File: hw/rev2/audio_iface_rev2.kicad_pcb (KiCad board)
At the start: 4 copper layers, 66 x 24.8 mm, 151 parts, among them J1 COAX, J2 CONN_01X02, J3 USBMICROCONN, J4 CONN_01X02, J5 CONN_01X02, J6 COAX, J7 COAX, J9 CONN_01X02, P3 CONN_01X06, U1 LT6241, U2 LTC6242, U3 AK4621, U4 K20X7_QFP64, U5 TPS61252, U6 LP2992AILD-5.0, U7 LTC6242, U8 TPA6130A2, U9 MT29FXX01A, X1 XTAL, X2 ASFLM2-12.288MHZ

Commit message: More routing
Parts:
- added TP12: TP, lib:TP_HOLE, F.Cu at (198.5, 73.0)
- added TP13: TP, lib:TP_HOLE, F.Cu at (199.5, 76.7)
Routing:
- net AGND_IN: track 199.1 -> 195.0 mm, vias 63 -> 62
- net +5VA: track 124.4 -> 125.5 mm, vias 13 -> 15
- net VCOM_VRT: track 36.9 -> 37.8 mm
- net (no net): track 3.38 -> 3.49 mm, vias 4 -> 5
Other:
- board text added: "AGND"
- board text added: "VCOM"

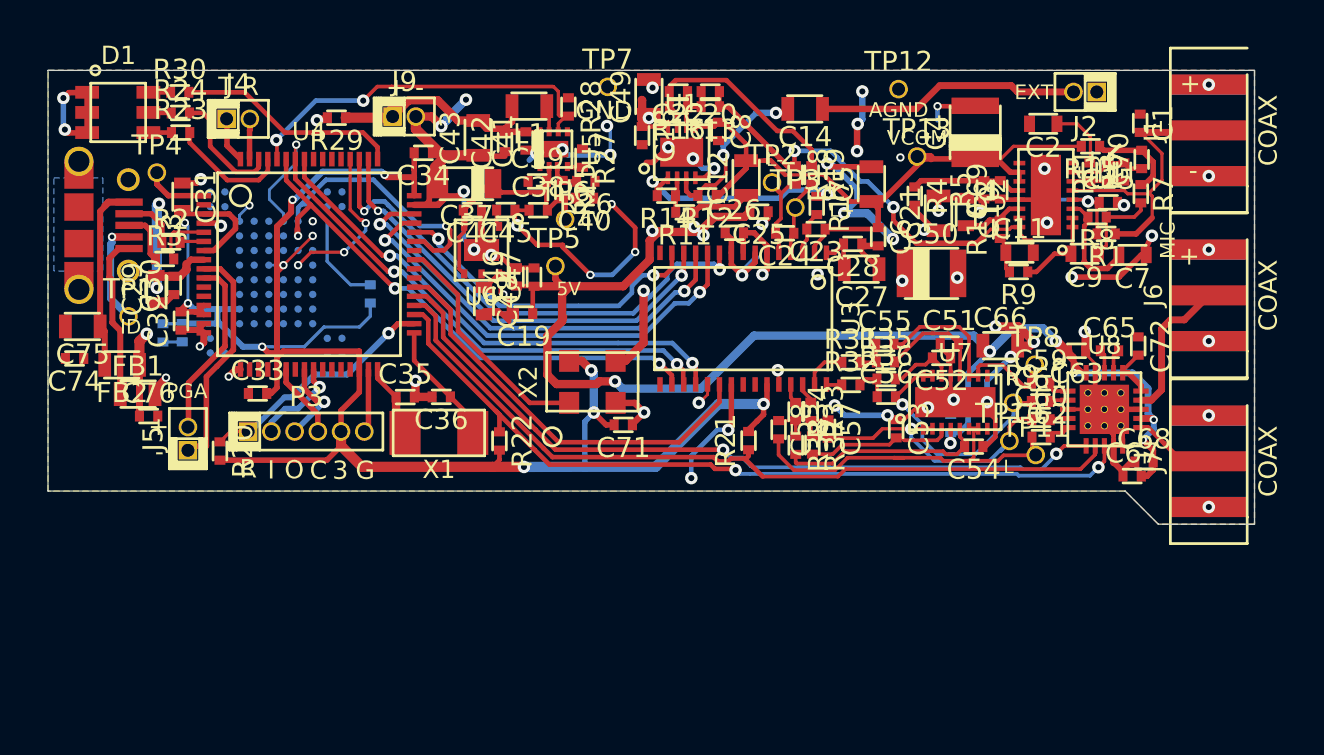
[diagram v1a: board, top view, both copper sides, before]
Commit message: Submitted PCB revision
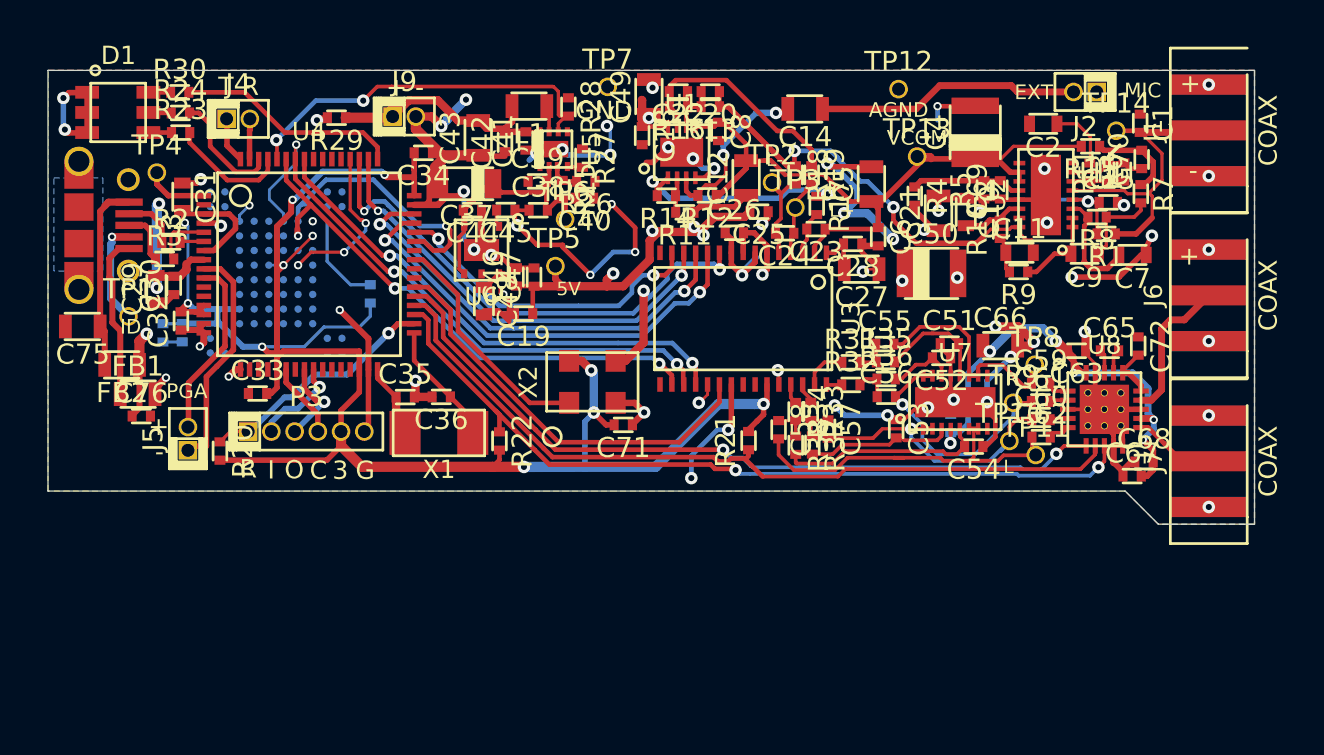
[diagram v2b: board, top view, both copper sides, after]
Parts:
- removed C74: 47p, lib:SMD0402
- added TP14: TP, lib:TP_HOLE, F.Cu at (210.4, 75.3)
- moved C76 0.40 mm to (157.1, 90.9)
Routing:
- net +5VA: track 125.5 -> 94.8 mm
- net AGND_IN: track 195.0 -> 199.8 mm, vias 62 -> 64
- net (no net): track 3.49 -> 0.00 mm, vias 5 -> 0
- net /Audio In/MIC_IN: track 16.0 -> 17.4 mm
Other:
- board text added: "AudioPulse rev3b 2016"
- board text removed: "AudioPulse rev3a 2015"

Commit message: Started wacky transition to Atmel's SAM S70N
For, you know, more hootz
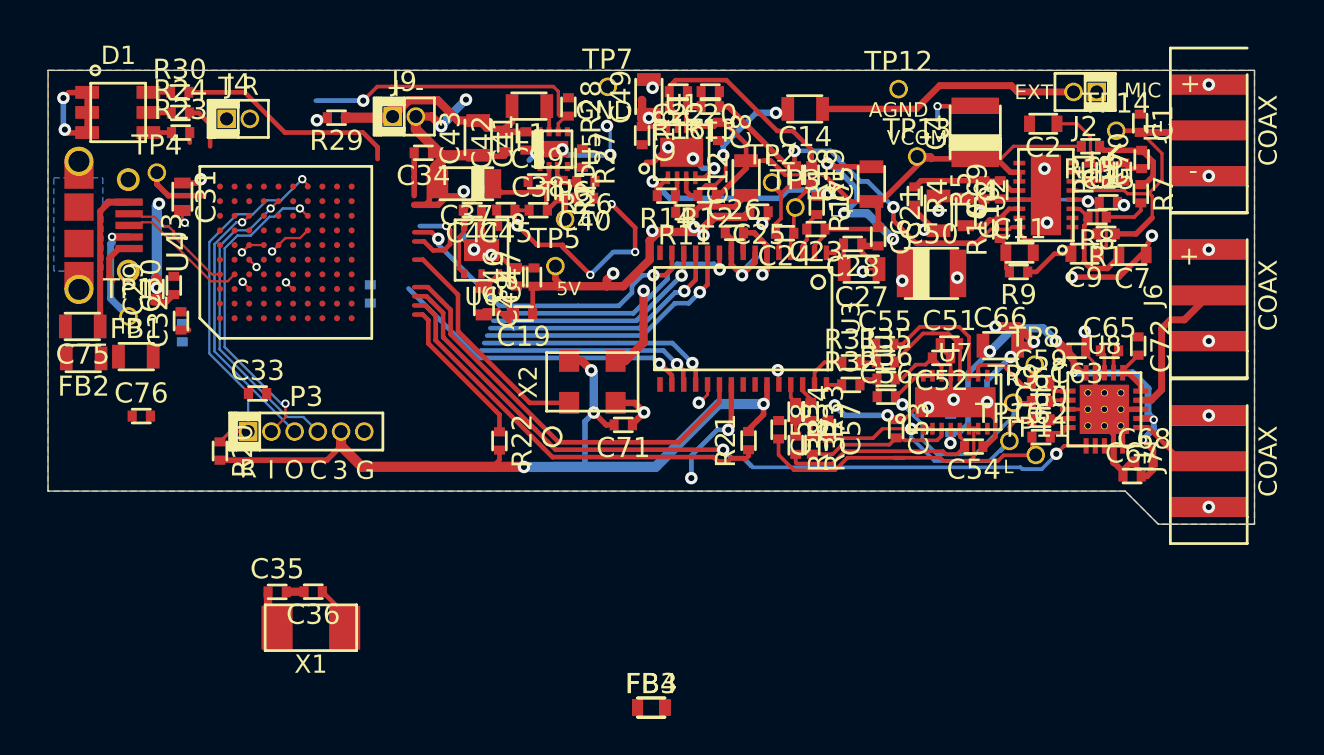
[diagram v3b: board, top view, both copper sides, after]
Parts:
- removed C73: 1u, lib:SMD0402
- removed J5: CONN_01X02, lib:HDR_2X1_50MIL
- removed R2, R3: 22R, lib:SMD0402
- removed U9: MT29FXX01A, MICRON_VFBGA63:MICRON_VFBGA63
- added FB3, FB4: BLM18PG471SN1D, lib:SMD0603, F.Cu at (185.0, 106.8)
- C16: value 0.1u -> 10n
- C29: value 2.2u -> 100n; footprint lib:SMD0603 -> lib:SMD0402
- C30: value 0.1u -> 10p
- C33: value 0.1u -> 100n
- R39: value 100k -> 5.62k
- U4: value K20X7_QFP64 -> SAM_S70N_TFBGA; footprint lib:FREESCALE_QFP64 -> lib:ATMEL_TFBGA100
- moved C35 12.7 mm to (164.5, 100.5)
- moved C36 12.7 mm to (166.5, 100.5)
- moved X1 12.7 mm to (166.4, 102.5)
- moved FB2 2.13 mm to (153.9, 87.8)
- moved FB1 2.05 mm to (156.8, 87.7)
- moved U4 1.43 mm to (165.0, 82.0), turned to 90 degrees
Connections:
- C29 pad 2: USB_5V -> Net-(C29-Pad2)
- C30 pad 2: USB_5V -> Net-(C30-Pad2)
- J3 pad 2: Net-(J3-Pad2) -> /USB_D_N
- J3 pad 3: Net-(J3-Pad3) -> /USB_D_P
- R21 pad 1: /Microcontroller/I2C_SDA -> /Microcontroller/I2C_SCL
- R22 pad 1: /Microcontroller/I2C_SCL -> /Microcontroller/I2C_SDA
- R23 pad 2: Net-(R23-Pad2) -> (no net)
- R24 pad 2: Net-(R24-Pad2) -> (no net)
- R30 pad 2: Net-(R30-Pad2) -> (no net)
- R39 pad 1: /Microcontroller/SPI1_CS_FLASH -> AGND_IN
- R39 pad 2: +3V -> Net-(C30-Pad2)
- TP4 pad 1: Net-(TP4-Pad1) -> (no net)
- U3 pad 21: /Microcontroller/CODEC_PDN -> (no net)
- U8 pad 6: /Microcontroller/HP_~SD -> (no net)
- X2 pad 1: Net-(U4-Pad41) -> (no net)
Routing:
- net (no net): track 0.00 -> 101.6 mm, vias 0 -> 3
- net +3V: track 110.7 -> 52.4 mm, vias 11 -> 8
- net /Microcontroller/HP_~SD: track 42.0 -> 0.00 mm, vias 2 -> 0
- net /Microcontroller/I2C_SDA: track 43.6 -> 8.62 mm
- net /Microcontroller/CODEC_PDN: track 22.9 -> 0.00 mm
- net /Microcontroller/I2C_SCL: track 44.5 -> 23.1 mm, vias 2 -> 0
- net /Microcontroller/SPI1_SCK: track 33.3 -> 12.3 mm, vias 3 -> 1
- net /Microcontroller/SPI1_CS_FLASH: track 20.8 -> 0.00 mm, vias 1 -> 0
- net AGND_IN: track 199.8 -> 184.1 mm, vias 64 -> 56
- net USB_5V: track 16.4 -> 0.72 mm, vias 4 -> 1
- net /Microcontroller/SPI1_CS_CODEC: track 27.7 -> 13.1 mm, vias 2 -> 1
- net /Microcontroller/SWCLK: track 4.11 -> 17.1 mm, vias 0 -> 1
- net /Microcontroller/CODEC_MCLK: track 32.8 -> 19.8 mm, vias 3 -> 2
- net Net-(U4-Pad41): track 12.9 -> 0.00 mm
- net /Microcontroller/PGA0_D+: track 12.6 -> 0.00 mm
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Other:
- board text removed: "PGA"

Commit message: Added 3V regulator, started wiring
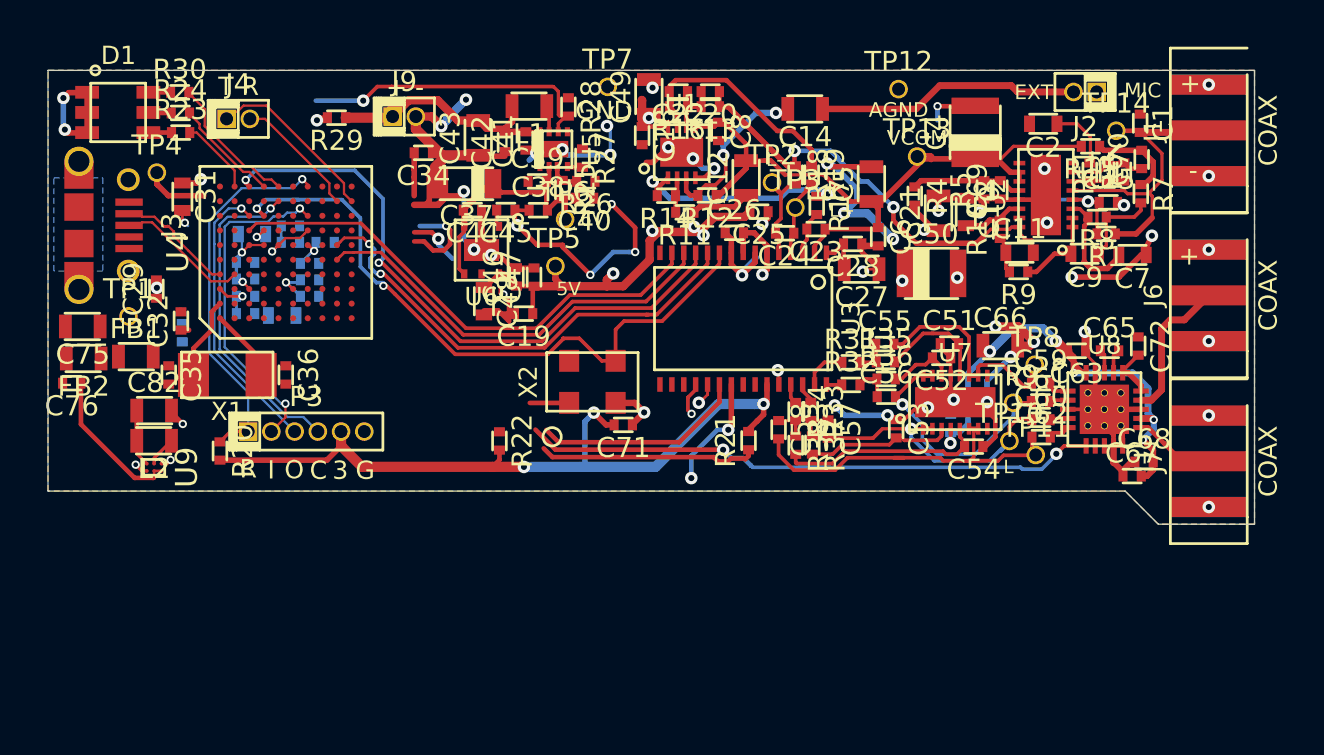
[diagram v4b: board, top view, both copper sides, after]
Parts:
- added C73: 100n, lib:SMD0402, B.Cu at (166.3, 83.5)
- added C74: 100n, lib:SMD0402, B.Cu at (165.2, 80.5)
- added C77: 100n, lib:SMD0402, B.Cu at (165.2, 81.4)
- added C78: 100n, lib:SMD0402, B.Cu at (162.8, 82.5)
- added C79: 100n, lib:SMD0402, B.Cu at (167.2, 81.4)
- added C80: 100n, lib:SMD0402, B.Cu at (162.8, 83.4)
- added C81: 100n, lib:SMD0402, B.Cu at (166.3, 82.5)
- added C82: 10u 6.3V, lib:SMD0805, F.Cu at (157.8, 90.6)
- added L2: MLZ2012A1R5WT000, lib:SMD0805, F.Cu at (157.8, 92.2)
- added U9: FAN536xx, lib:FAN53600_WLCSP6, F.Cu at (157.8, 93.7)
- C30, C33, FB3, FB4: moved to B.Cu
- C34: value 10n -> 100n
- X1: value XTAL -> 7A-16.000MAAJ-T
- moved FB4 33.9 mm to (163.2, 81.0)
- moved FB3 29.4 mm to (164.8, 85.4), turned to 180 degrees
- moved X1 14.6 mm to (161.8, 88.7)
- moved C35 13.3 mm to (158.6, 88.7), turned to 270 degrees
- moved C36 11.9 mm to (165.0, 88.7), turned to 270 degrees
- moved R39 6.90 mm to (162.8, 85.3), turned to 180 degrees
- moved C33 6.03 mm to (166.3, 84.3), turned to 180 degrees
- moved C76 4.20 mm to (153.3, 89.1), turned to 180 degrees
- moved C30 3.97 mm to (162.8, 84.3), turned to 180 degrees
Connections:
- R23 pad 2: (no net) -> /Microcontroller/LED1
- R24 pad 2: (no net) -> /Microcontroller/LED2
- R30 pad 2: (no net) -> /Microcontroller/LED3
- U4 pad B10: (no net) -> /Microcontroller/LED1
- U4 pad D10: (no net) -> /Microcontroller/LED2
- U4 pad E10: (no net) -> /Microcontroller/LED3
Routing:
- net (no net): track 101.6 -> 53.7 mm, vias 3 -> 4
- net /CODEC/BICK: track 13.8 -> 33.9 mm, vias 1 -> 2
- net /Microcontroller/SPI1_SOUT: track 16.9 -> 0.00 mm, vias 1 -> 0
- net /Microcontroller/CODEC_MCLK: track 19.8 -> 36.2 mm
- net /Microcontroller/CODEC_SDO: track 17.9 -> 30.6 mm, vias 2 -> 1
- net /Microcontroller/SPI1_SCK: track 12.3 -> 0.04 mm, vias 1 -> 0
- net /Microcontroller/CODEC_LRCK: track 14.9 -> 26.8 mm, vias 1 -> 2
- net /Microcontroller/SPI1_CS_CODEC: track 13.1 -> 1.86 mm
- net /Microcontroller/I2C_SCL: track 23.1 -> 12.0 mm
- net /Microcontroller/CODEC_SDIN: track 12.6 -> 23.2 mm, vias 1 -> 0
- net /Microcontroller/UART0_TX: track 0.00 -> 9.63 mm
- net Net-(C75-Pad1): track 9.50 -> 0.00 mm
- net /Microcontroller/I2C_SDA: track 8.62 -> 0.00 mm
- net USB_5V: track 0.72 -> 8.90 mm
- net /Microcontroller/LED3: track 0.00 -> 7.61 mm
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
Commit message: Fully routed
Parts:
- removed TP4: TP_PTE0, lib:TP_HOLE
- C29, C32: moved to B.Cu
- moved C32 7.08 mm to (166.3, 86.5), turned to 180 degrees
- moved C29 6.71 mm to (164.5, 82.6), turned to 180 degrees
- moved C16 5.58 mm to (164.5, 84.3), turned to 0 degrees
- moved C34 4.86 mm to (167.7, 76.0)
- moved C35 2.35 mm to (159.1, 86.4), turned to 180 degrees
- moved C72 1.72 mm to (210.0, 86.4), turned to 0 degrees
- moved C79 1.58 mm to (167.6, 82.9), turned to 90 degrees
- moved X1 0.13 mm to (161.8, 88.5)
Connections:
- U3 pad 21: (no net) -> /Microcontroller/CODEC_PDN
- U4 pad B10: /Microcontroller/LED1 -> (no net)
- U4 pad D10: /Microcontroller/LED2 -> /Microcontroller/LED1
- U4 pad D9: (no net) -> /Microcontroller/LED2
- U4 pad E10: /Microcontroller/LED3 -> (no net)
- U4 pad H1: (no net) -> /Microcontroller/CLK_EN
- U4 pad J1: (no net) -> /Microcontroller/CODEC_PDN
- U4 pad J10: (no net) -> /Microcontroller/ANALOG_EN
- U4 pad K1: (no net) -> /Microcontroller/HP_~SD
- U4 pad K10: (no net) -> /Microcontroller/LED3
- U8 pad 6: (no net) -> /Microcontroller/HP_~SD
- X2 pad 1: (no net) -> /Microcontroller/CLK_EN
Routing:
- net /Microcontroller/I2C_SDA: track 0.00 -> 54.6 mm, vias 0 -> 2
- net (no net): track 53.7 -> 0.00 mm, vias 4 -> 0
- net /Microcontroller/I2C_SCL: track 12.0 -> 58.2 mm, vias 0 -> 4
- net /Microcontroller/HP_~SD: track 0.00 -> 44.4 mm, vias 0 -> 4
- net /Microcontroller/CODEC_PDN: track 0.00 -> 25.3 mm, vias 0 -> 2
- net /Microcontroller/SPI1_CS_CODEC: track 1.86 -> 25.4 mm, vias 1 -> 0
- net /Microcontroller/SPI1_SOUT: track 0.00 -> 22.8 mm
- net /Microcontroller/SPI1_SCK: track 0.04 -> 22.5 mm
- net AGND_IN: track 184.1 -> 201.4 mm, vias 59 -> 71
- net /Microcontroller/CLK_EN: track 0.00 -> 16.7 mm, vias 0 -> 2
- net Net-(C75-Pad1): track 0.00 -> 11.0 mm
- net +1V2: track 6.15 -> 14.4 mm, vias 3 -> 2
- net Net-(FB1-Pad1): track 0.55 -> 7.49 mm
- net +3V: track 54.7 -> 60.7 mm, vias 6 -> 12
- net Net-(J3-Pad4): track 0.00 -> 5.92 mm
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- added copper zone on Inner2.Cu, net +3V
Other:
- net class Default: clearance 0.1524 -> 0.127; trace_width 0.1524 -> 0.127; via_dia 0.6858 -> 0.4572; via_drill 0.3302 -> 0.254
- rule trace_clearance: 0.1524 -> 0.127

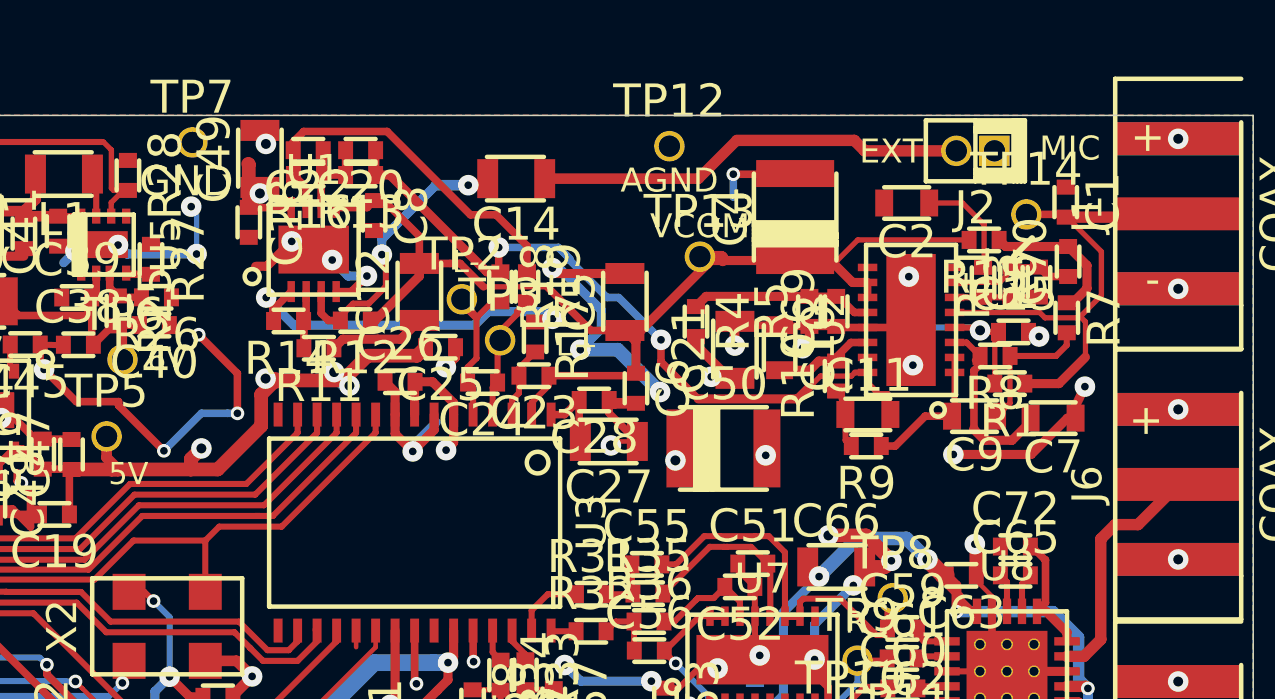
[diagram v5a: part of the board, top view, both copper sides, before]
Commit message: Simplified input processing, reduced amp count by 2
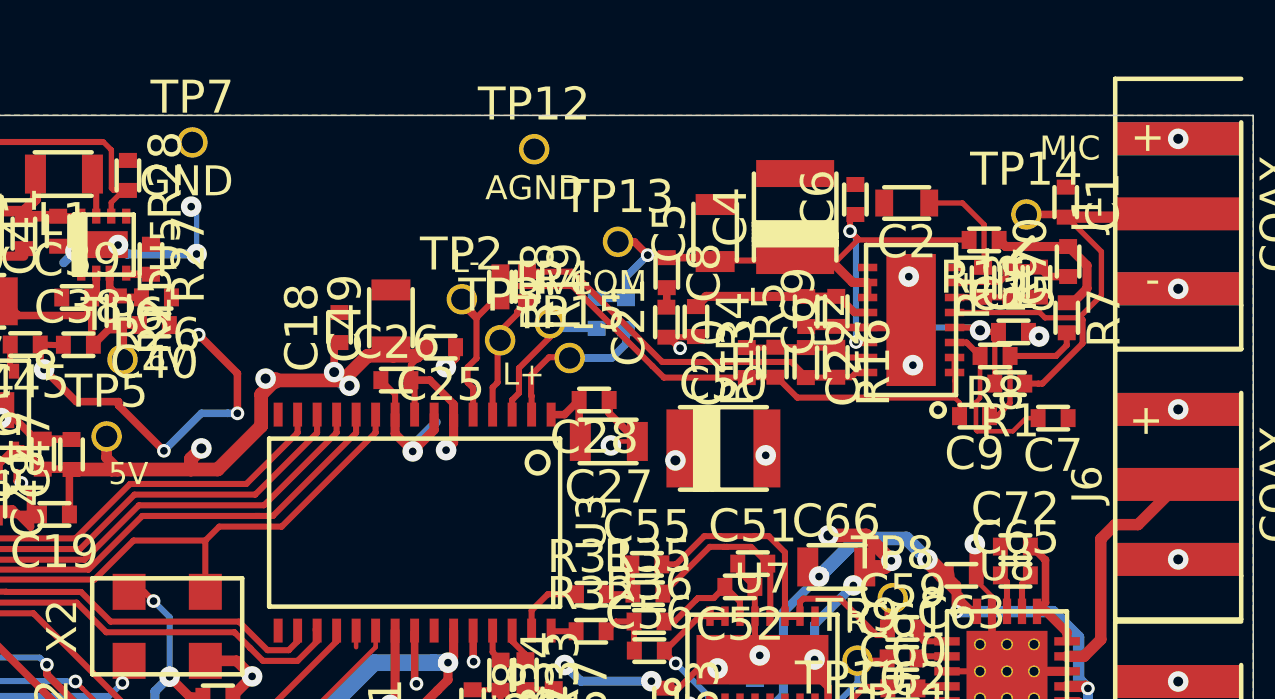
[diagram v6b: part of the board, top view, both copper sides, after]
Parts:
- removed C10: 1n, lib:SMD0603
- removed C11: 33n, lib:SMD0603
- removed C12, C14: 10u 6.3V, lib:SMD0805
- removed C23, C24: 10n, lib:SMD0402
- removed J2: CONN_01X02, lib:HDR_2X1_50MIL
- removed R10: 4.53k (1%), lib:SMD0402
- removed R11, R14: 220 (1%), lib:SMD0402
- removed R12: 250k, lib:SMD0402
- removed R17: 22, lib:SMD0402
- removed R9: 1.4k (1%), lib:SMD0402
- removed U1: LT6241, lib:LT_DFN8_DUAL
- added R2: 0, lib:SMD0402, B.Cu at (196.1, 78.6)
- added R3: 0, lib:SMD0402, B.Cu at (197.1, 78.6)
- added TP15: TP, lib:TP_HOLE, F.Cu at (195.2, 80.1)
- added TP4: TP, lib:TP_HOLE, F.Cu at (194.5, 78.9)
- C21: value 10u 6.3V -> 1u 6.3V; footprint lib:SMD0805 -> lib:SMD0402
- C7, C9: footprint lib:SMD0603 -> lib:SMD0402
- moved R16 18.7 mm to (204.1, 80.2), turned to 270 degrees
- moved C22 18.0 mm to (203.0, 80.2), turned to 270 degrees
- moved R13 15.2 mm to (202.0, 80.2), turned to 90 degrees
- moved C20 14.7 mm to (201.1, 80.2), turned to 90 degrees
- moved C8 9.94 mm to (198.4, 77.2)
- moved C6 9.65 mm to (204.7, 74.8), turned to 90 degrees
- moved C49 6.88 mm to (189.2, 78.8)
- moved C18 4.63 mm to (187.5, 79.1), turned to 90 degrees
- moved TP12 4.51 mm to (194.0, 73.1)
- moved C5 3.79 mm to (200.0, 75.9)
- moved TP13 2.78 mm to (196.8, 76.2)
- moved C21 2.46 mm to (198.4, 78.9)
- moved C26 0.15 mm to (189.4, 80.8)
- moved R5 0.11 mm to (203.1, 78.5)
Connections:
- C20 pad 1: Net-(C11-Pad2) -> Net-(C20-Pad1)
- C9 pad 2: Net-(C9-Pad2) -> Net-(C20-Pad1)
- R13 pad 1: Net-(C11-Pad2) -> Net-(C20-Pad1)
- R18 pad 1: Net-(C11-Pad2) -> Net-(C20-Pad1)
- U2 pad n1: Net-(C9-Pad2) -> Net-(C20-Pad1)
- U2 pad n4: Net-(C11-Pad2) -> Net-(C20-Pad2)
- U2 pad o1: Net-(C9-Pad2) -> Net-(C20-Pad1)
- U2 pad o4: Net-(C11-Pad2) -> Net-(C22-Pad2)
- U2 pad p4: Net-(C10-Pad2) -> VCOM_VRT
- U3 pad 2: VCOM_VRT -> /CODEC/AINR+
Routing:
- net AGND_IN: track 201.4 -> 170.5 mm, vias 71 -> 59
- net Net-(C11-Pad2): track 24.7 -> 0.00 mm, vias 2 -> 0
- net Net-(C20-Pad1): track 0.00 -> 19.0 mm
- net /Audio In/EXT_IN: track 14.4 -> 0.00 mm
- net VCOM_VRT: track 37.8 -> 23.4 mm, vias 0 -> 3
- net Net-(R14-Pad2): track 12.9 -> 0.00 mm, vias 2 -> 0
- net Net-(C14-Pad2): track 10.7 -> 0.00 mm, vias 2 -> 0
- net /CODEC/AINR+: track 0.00 -> 5.44 mm
- net Net-(C9-Pad2): track 4.76 -> 0.00 mm
- net Net-(C10-Pad2): track 3.39 -> 0.00 mm
- net Net-(C12-Pad1): track 3.23 -> 0.00 mm
- net /CODEC/AINR-: track 2.41 -> 5.19 mm
- net Net-(C11-Pad1): track 2.06 -> 0.00 mm
- net +5VA: track 94.8 -> 92.8 mm, vias 15 -> 14
- net Net-(R11-Pad2): track 1.93 -> 0.00 mm
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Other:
- board text added: "AudioPulse rev3 2016"
- board text removed: "AudioPulse rev3b 2016"
- board text removed: "EXT"

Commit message: Finished simlified design
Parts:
- moved R16 0.12 mm to (203.9, 80.2)
